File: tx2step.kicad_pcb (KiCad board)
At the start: 2 copper layers, 86.4 x 31.8 mm, 65 parts, among them CON1 BARREL_JACK, IC1 TPS2113A, IC2 MCP73831, IC3 TPS61202, IC4 DRV8834, IC5 DRV8834, J1 Prog, J2 8P8C, J3 CHASSIS_SWITCHES, J4 6P4Cx2, SW1 SW_DIP_x02, U1 ATmega328P-MMH, Y1 16 MHz

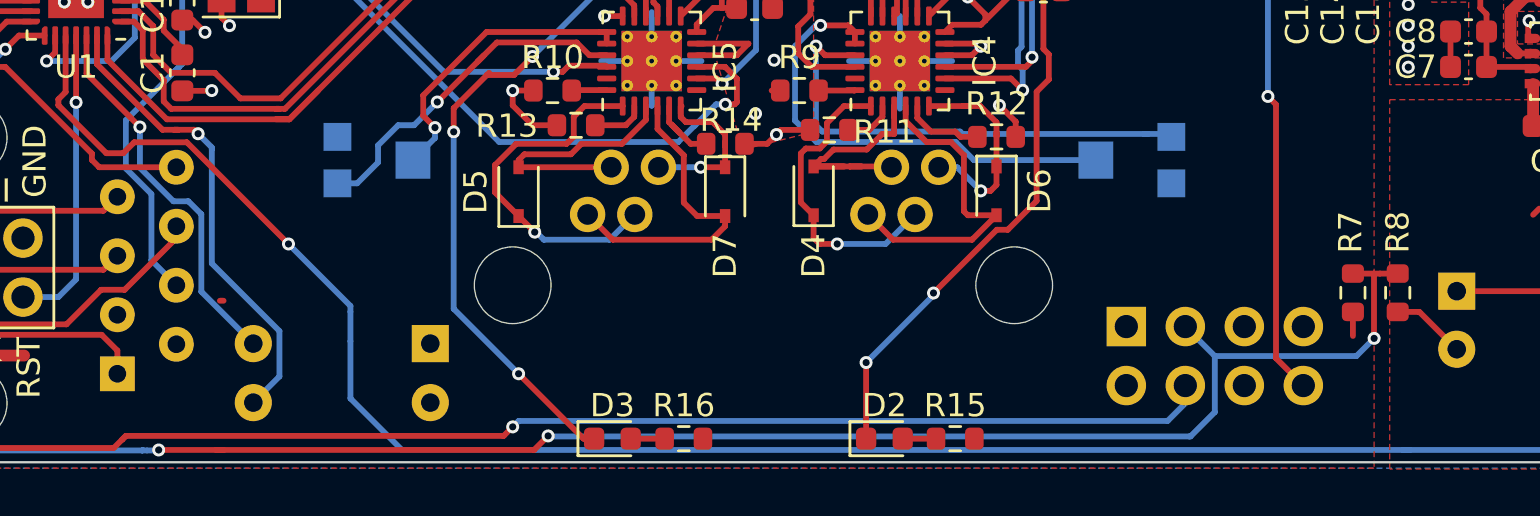
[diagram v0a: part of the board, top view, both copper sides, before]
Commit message: Additional silkscreen legends
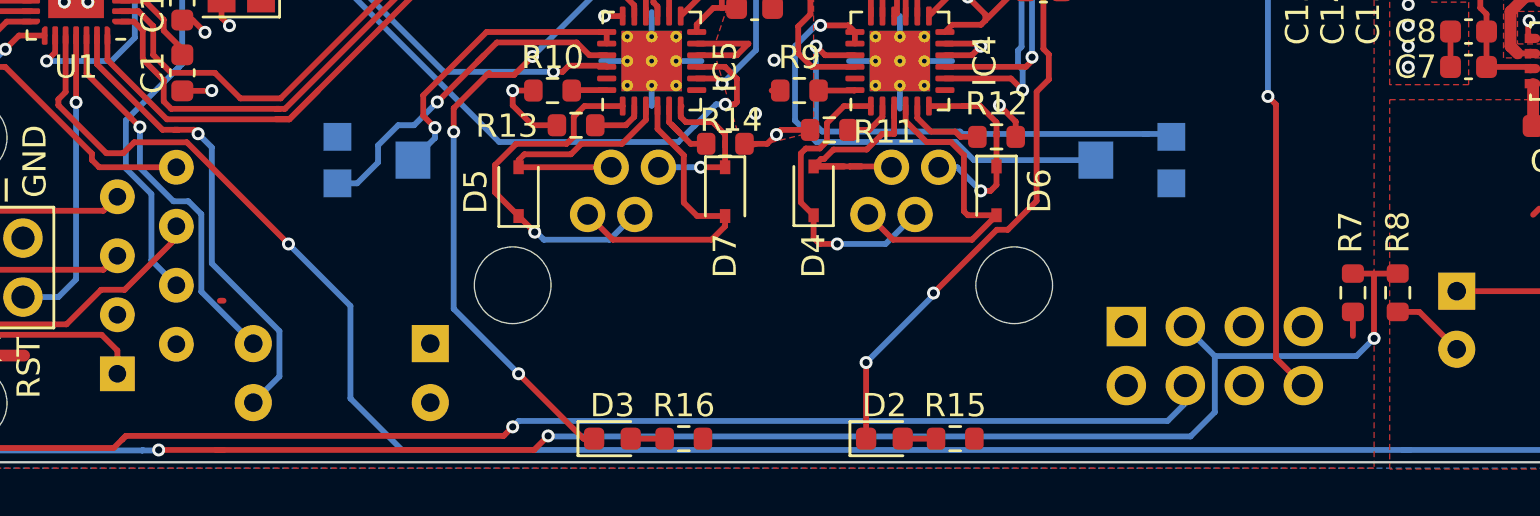
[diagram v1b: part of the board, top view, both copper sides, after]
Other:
- board text added: "DEC PWR"
- board text added: "EQ3"
- board text added: "EQ5"
- board text added: "N"
- board text added: "RA PWR"
- board text added: "S"

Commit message: more rerouting and cleanup
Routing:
- net /JS_RA: track 33.2 -> 40.6 mm
- net /POWER_LED: track 33.5 -> 40.6 mm
- net VCC: track 45.0 -> 38.8 mm
- net /GUIDE_RATE: track 83.9 -> 86.8 mm, vias 5 -> 3
- net /DEC_DIR: track 38.8 -> 36.9 mm
- net /JS_DEC: track 15.0 -> 16.9 mm
- net /RA_STEP: track 60.4 -> 59.1 mm
- net /DEC_PWR: track 29.2 -> 28.0 mm
- net /MUX_STAT: track 97.8 -> 96.6 mm
- net /CHARGE_STAT: track 95.9 -> 97.0 mm
- net /DEC_STEP: track 39.2 -> 38.5 mm
- net /ST4_DEC-: track 48.3 -> 47.6 mm
- net /DC_SENSE: track 83.0 -> 82.4 mm
- net Net-(D2-Pad1): track 29.4 -> 29.2 mm, vias 2 -> 0

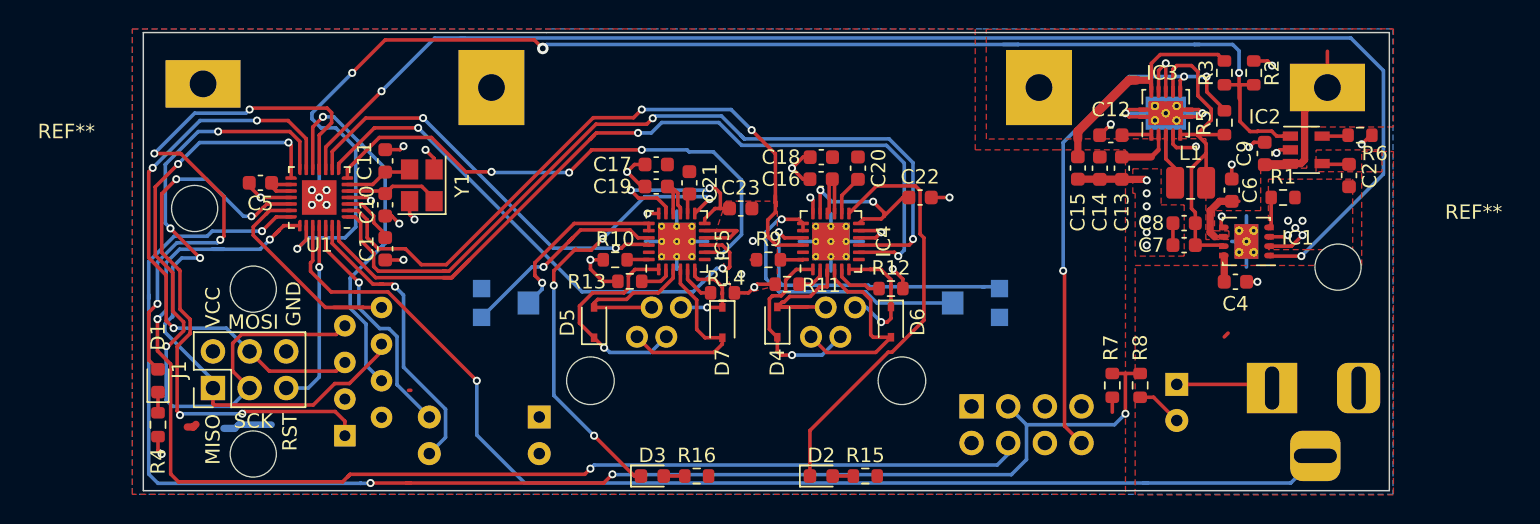
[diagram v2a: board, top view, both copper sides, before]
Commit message: Improve DRV8845 xISEN resistor courtyard clearances; fully connect thermal pads
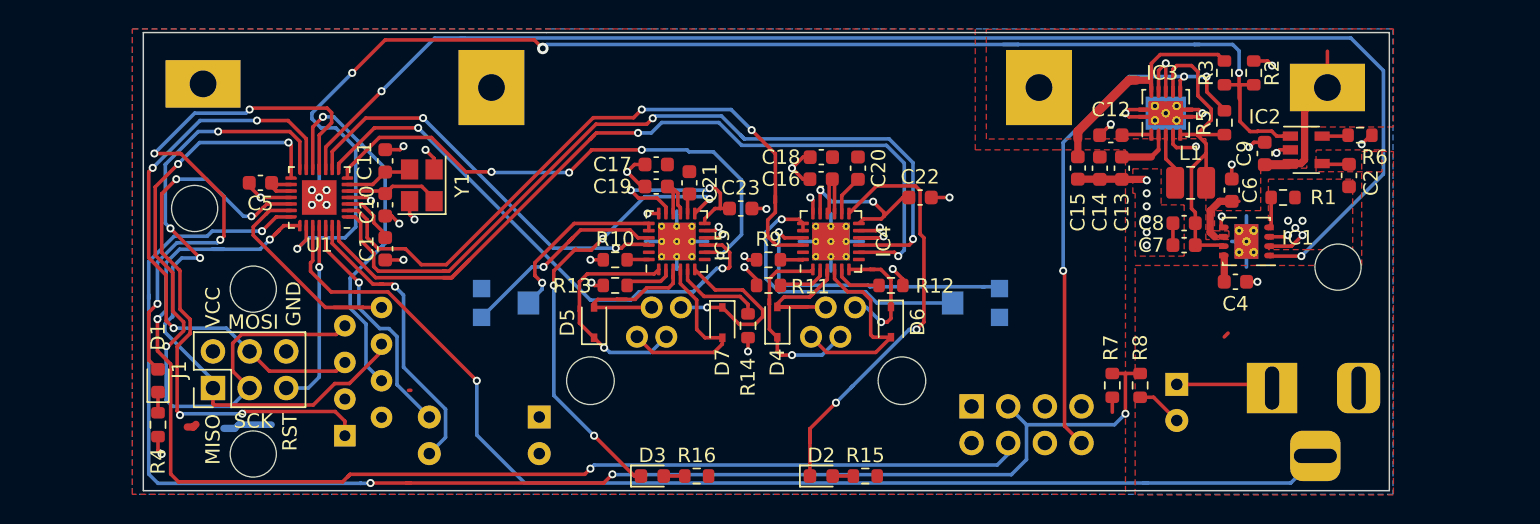
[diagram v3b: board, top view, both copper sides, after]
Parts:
- moved R14 2.88 mm to (150.4, 78.0), turned to 90 degrees
- moved R11 1.29 mm to (151.8, 75.2)
- moved R13 1.05 mm to (141.2, 75.2)
- moved R12 0.22 mm to (160.3, 75.2)
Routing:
- net GND: track 113.7 -> 104.0 mm, vias 47 -> 52
- net Net-(D7-Pad1): track 7.35 -> 12.7 mm
- net Net-(IC5-Pad5): track 3.13 -> 6.02 mm
- net /DEC_DIR: track 36.9 -> 38.7 mm
- net Net-(D2-Pad1): track 29.2 -> 30.8 mm, vias 0 -> 2
- net Net-(IC4-Pad2): track 2.16 -> 3.48 mm
- net Net-(IC5-Pad2): track 2.29 -> 3.42 mm
- net Net-(D5-Pad2): track 11.1 -> 12.1 mm
- net Net-(D5-Pad1): track 15.5 -> 16.4 mm
- net Net-(D4-Pad1): track 13.2 -> 13.9 mm

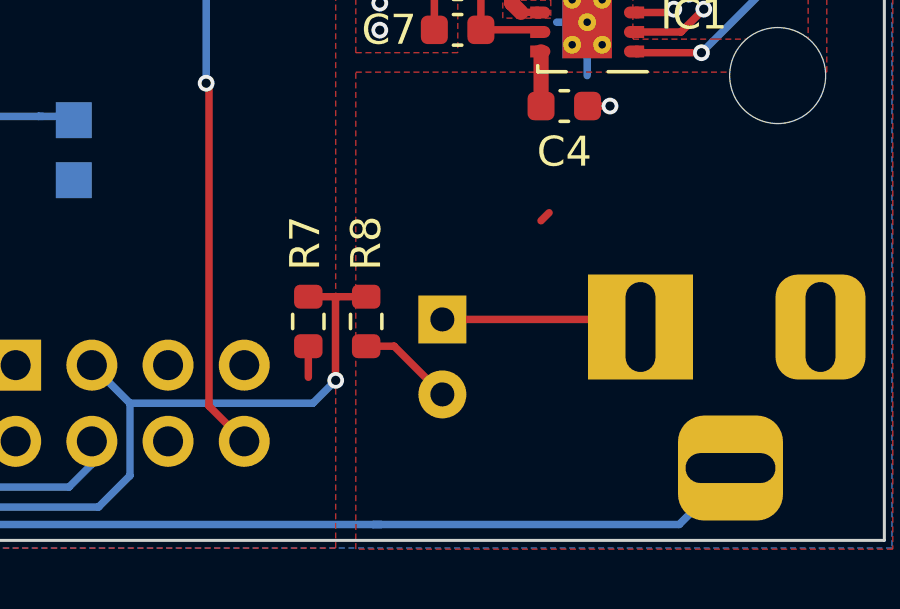
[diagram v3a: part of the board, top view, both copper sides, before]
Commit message: Use smaller footprint for THT capacitor
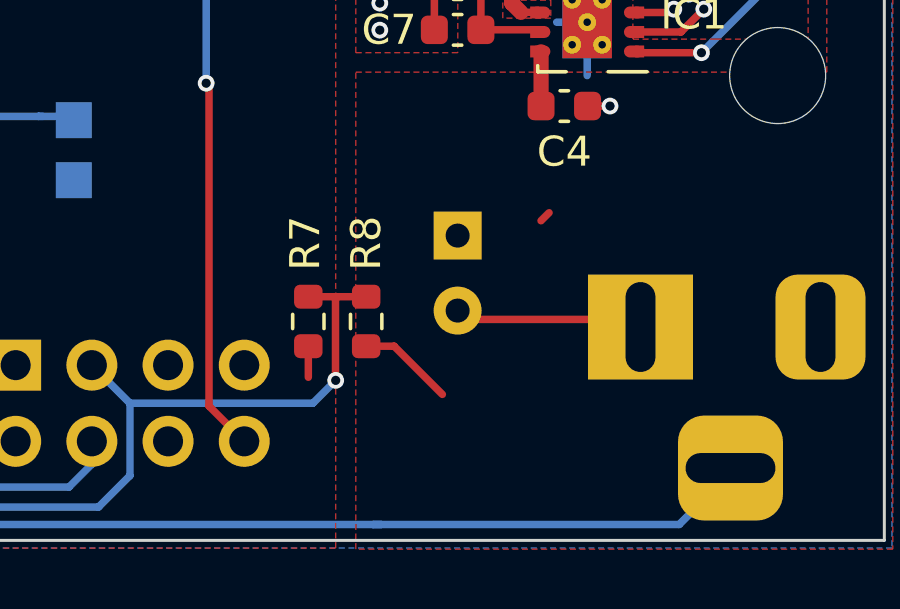
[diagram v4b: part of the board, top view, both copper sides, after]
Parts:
- moved C3 2.84 mm to (180.6, 79.2)
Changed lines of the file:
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@@
   )
   (module Capacitor_THT:CP_Radial_D6.3mm_P2.50mm (layer B.Cu)
-    (at 180.086 82.042 270)
+    (at 180.594 79.248 270)
     (descr "CP, Radial series, Radial, pin pitch=2.50mm, , diameter=6.3mm, Electrolytic Capacitor")
     (tags "CP Radial series Radial pin pitch 2.50mm  diameter 6.3mm Electrolytic Capacitor")

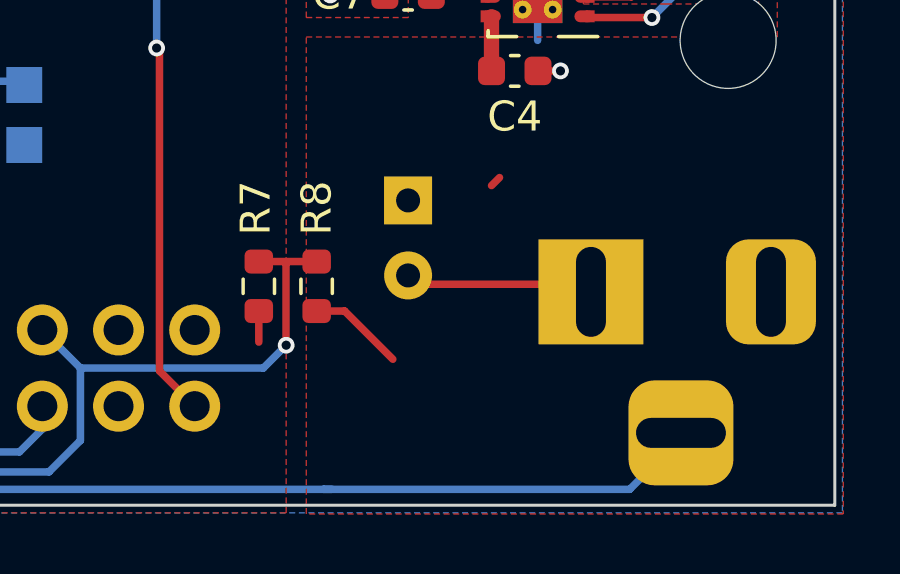
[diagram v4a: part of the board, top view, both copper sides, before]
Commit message: move silkscreen to avoid collision
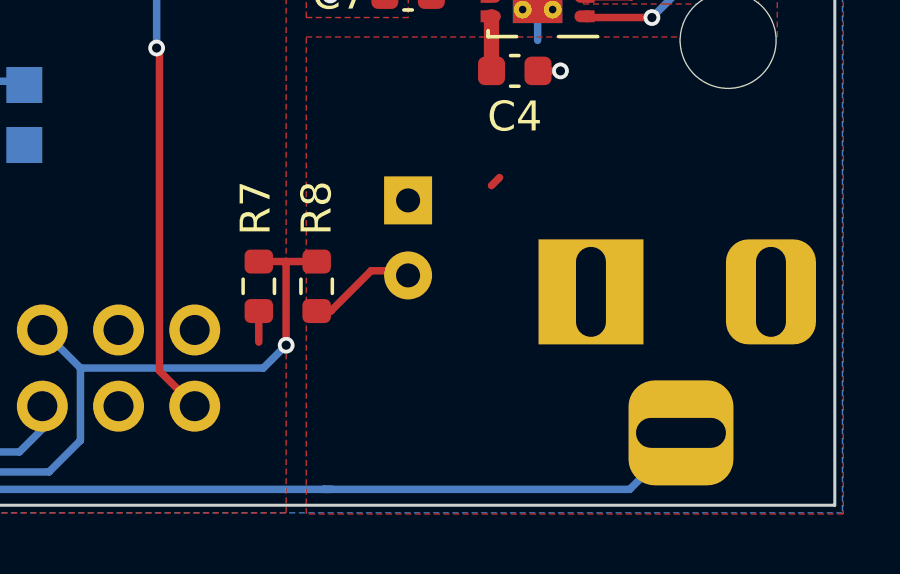
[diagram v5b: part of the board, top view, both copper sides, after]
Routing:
- net +5V: track 10.8 -> 4.45 mm
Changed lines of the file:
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@@
     (effects (font (size 1 1) (thickness 0.15)))
   )
-  (gr_text "Texas Two Step rev. 0.1\nαLyraen Astronomy" (at 178.816 73.914) (layer B.SilkS)
+  (gr_text "Texas Two Step rev. 0.1\nαLyraen Astronomy" (at 178.562 74.93) (layer B.SilkS)
     (effects (font (size 1 1) (thickness 0.15)) (justify mirror))
   )
@@
   (segment (start 109.474 85.661) (end 109.474 86.614) (width 0.25) (layer F.Cu) (net 1) (status 10))
   (segment (start 109.474 86.614) (end 109.728 86.868) (width 0.25) (layer F.Cu) (net 1))
-  (segment (start 178.479099 82.935099) (end 180.086 84.542) (width 0.25) (layer F.Cu) (net 1) (status 20))
-  (segment (start 177.546 82.935099) (end 178.479099 82.935099) (width 0.25) (layer F.Cu) (net 1) (status 10))
   (via (at 179.324 59.7864) (size 0.5588) (drill 0.3048) (layers F.Cu B.Cu) (net 1))
   (segment (start 179.324 61.771) (end 179.324 59.7864) (width 0.25) (layer F.Cu) (net 1) (status 10))
@@
   (via (at 150.368 79.756) (size 0.5588) (drill 0.3048) (layers F.Cu B.Cu) (net 1))
   (segment (start 150.368 78.549) (end 150.368 79.756) (width 0.25) (layer F.Cu) (net 1))
+  (segment (start 179.364109 81.59199) (end 180.594 81.59199) (width 0.25) (layer F.Cu) (net 1))
+  (segment (start 178.021 82.935099) (end 179.364109 81.59199) (width 0.25) (layer F.Cu) (net 1))
+  (segment (start 177.546 82.935099) (end 178.021 82.935099) (width 0.25) (layer F.Cu) (net 1))
   (segment (start 189.23 62.7634) (end 190.5254 61.468) (width 0.25) (layer F.Cu) (net 2) (status 30))
   (segment (start 187.881 66.815) (end 187.96 66.736) (width 0.25) (layer F.Cu) (net 2) (status 30))
@@
   (segment (start 192.024 66.789) (end 190.213 66.789) (width 0.25) (layer F.Cu) (net 4) (status 30))
   (segment (start 186.436 82.042) (end 186.69 82.296) (width 0.25) (layer F.Cu) (net 4) (status 30))
-  (segment (start 180.086 82.042) (end 186.436 82.042) (width 0.25) (layer F.Cu) (net 4) (status 30))
   (segment (start 183.375 73.124) (end 183.362 73.111) (width 0.25) (layer F.Cu) (net 4) (status 30))
   (segment (start 183.375 74.93) (end 183.375 73.124) (width 0.508) (layer F.Cu) (net 4) (status 30))

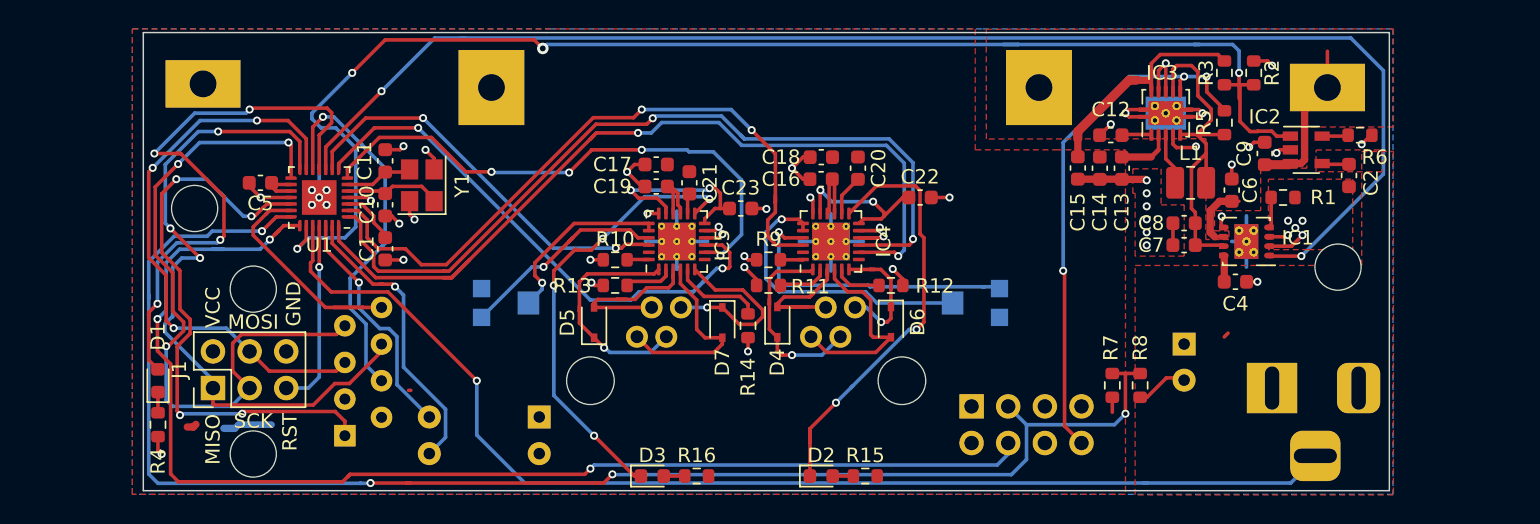
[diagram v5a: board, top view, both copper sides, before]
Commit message: move isen; use pulldown
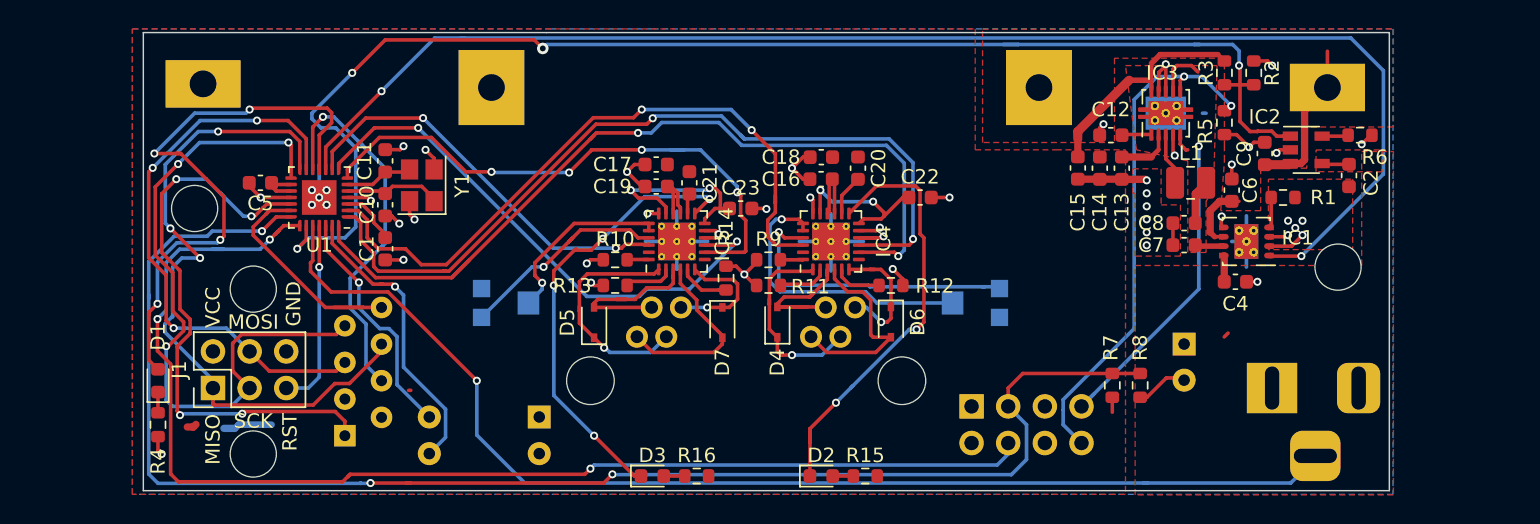
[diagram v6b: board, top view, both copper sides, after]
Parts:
- R2, R3, R5, R7, R8: value 4.7KΩ -> 10KΩ
- R6: value 2Ω -> 2KΩ
- moved R14 3.64 mm to (148.8, 74.7), turned to 270 degrees
- turned R5 to 270 degrees
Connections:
- C7 pad 1: Net-(C7-Pad1) -> /REG_IN
- C8 pad 1: Net-(C7-Pad1) -> /REG_IN
- IC1 pad 7: Net-(C7-Pad1) -> /REG_IN
- IC3 pad 5: Net-(C7-Pad1) -> /REG_IN
- IC3 pad 7: Net-(C7-Pad1) -> /REG_IN
- J3 pad 7: GND -> /REG_IN
- L1 pad 2: Net-(C7-Pad1) -> /REG_IN
- R5 pad 1: Net-(C7-Pad1) -> /SW_POWER
- R5 pad 2: /SW_POWER -> GND
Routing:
- net /REG_IN: track 0.00 -> 32.8 mm, vias 0 -> 1
- net Net-(C7-Pad1): track 23.4 -> 0.00 mm
- net Net-(D7-Pad1): track 12.7 -> 8.59 mm
- net Net-(IC5-Pad5): track 6.02 -> 3.53 mm
- net /DEC_STEP: track 38.5 -> 39.8 mm
- net /TRACK_RATE: track 104.3 -> 103.3 mm, vias 4 -> 3
- net /DEC_DIR: track 38.7 -> 37.8 mm
- net /CHARGE_STAT: track 97.0 -> 96.0 mm
- net GND: track 104.4 -> 105.2 mm, vias 52 -> 47
- net /SW_POWER: track 37.3 -> 36.5 mm, vias 3 -> 2
- net Net-(D7-Pad2): track 13.7 -> 13.0 mm
- net /RA_STEP: track 59.1 -> 58.5 mm
- added copper zone on F.Cu, net /REG_IN
